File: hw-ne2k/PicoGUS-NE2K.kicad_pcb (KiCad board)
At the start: 2 copper layers, 103.7 x 74.1 mm, 46 parts, among them J1 2x5 header, J2 1x2 header, J3 Bus_ISA_8bit, J5 USB-A, J6 1x2 header, U1 Raspberry Pi Pico W, U10 74LVC2G06, U13 SST39SF010A, U14 74HCT688, U15 74AHCT245, U16 74AHCT1G08, U17 USBLC6-2SC6, U2 74LVC244, U3 SN74CB3T3257, U4 SN74CB3T3257, U5 74AHC14, U6 74LVC00, U7 74LVC1G00, U8 APS6404L-3SQR-SN

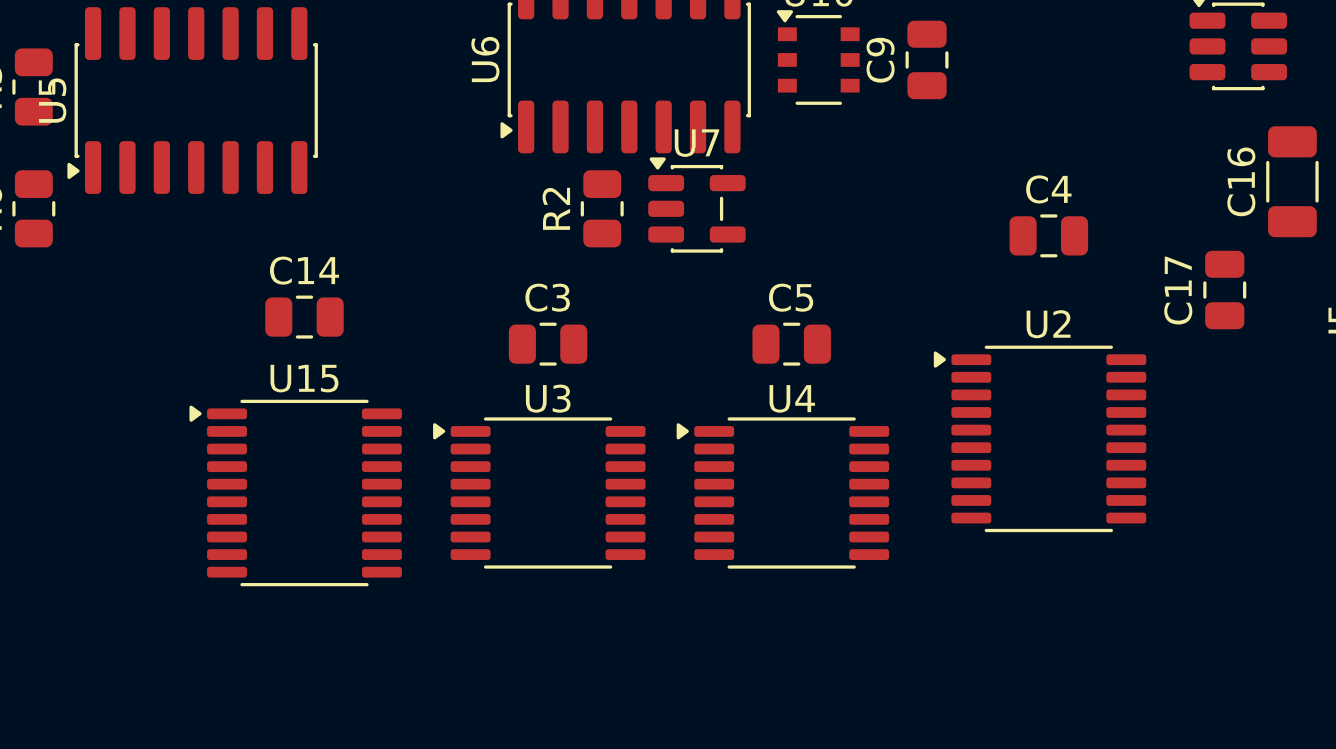
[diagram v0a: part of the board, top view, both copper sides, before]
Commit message: hw-ne2k: bus-switch row moved up/spread for routing escape (board re-routing)
Co-Authored-By: Claude Opus 5.5 <noreply@anthropic.com>
Claude-Session: https://claude.ai/code/session_011utN3x8yYUNDvkpGCEq5yD
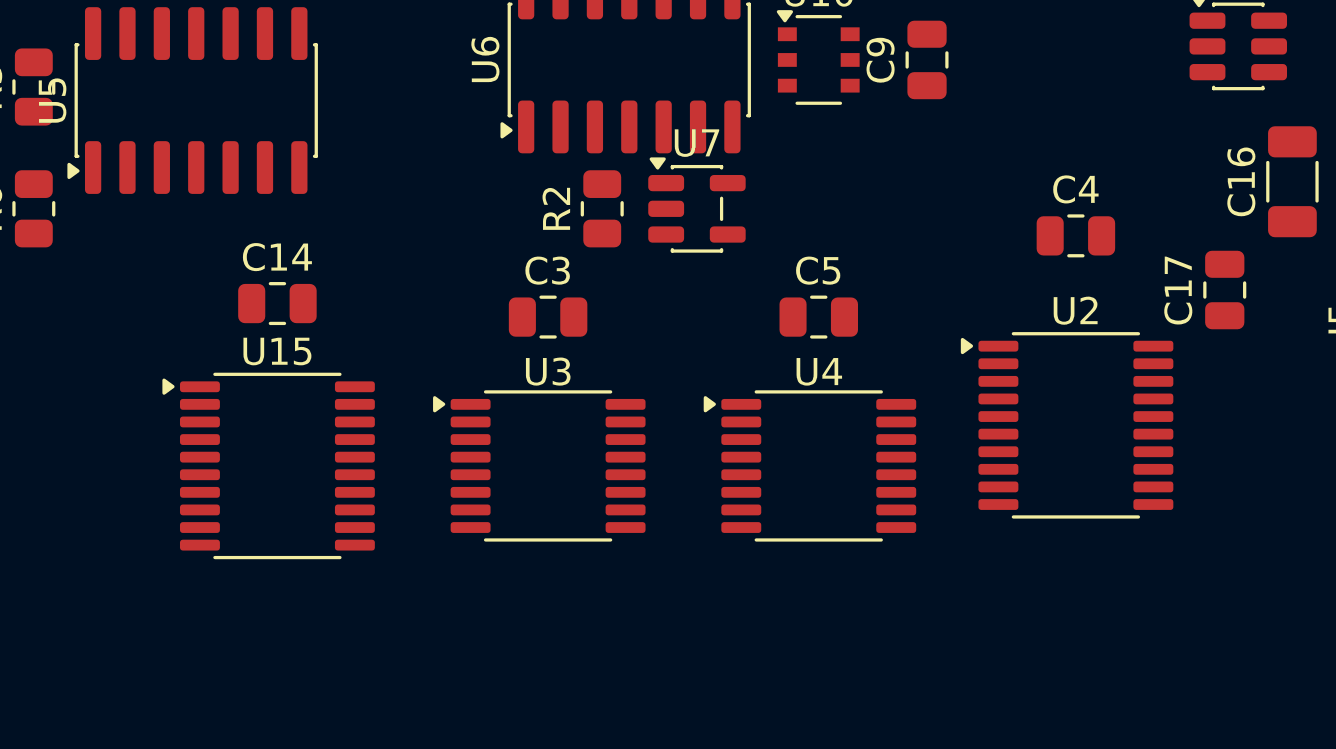
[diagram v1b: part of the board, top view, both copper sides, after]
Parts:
- moved C5 1.41 mm to (185.5, 109.5)
- moved U15 1.41 mm to (165.5, 115.0)
- moved U4 1.41 mm to (185.5, 115.0)
- moved C14 1.12 mm to (165.5, 109.0)
- moved U2 1.12 mm to (195.0, 113.5)
- moved C3 1.00 mm to (175.5, 109.5)
- moved C4 1.00 mm to (195.0, 106.5)
- moved U3 1.00 mm to (175.5, 115.0)

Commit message: hw-ne2k: routed board (DRC 0/0), silkscreen and artwork, README
- Freerouting + manual fix-ups: IRQ grid-routed, GND pour stitched (57
  vias) and U17 GND tied in. KiCad 10 DRC: 0 violations, 0 unconnected,
  schematic parity OK (warnings: 2 silk-to-edge at the USB-A, 3 thermals).
- No copper under the Pico W antenna or between its end and the bracket.
- Front silk: title, IRQ numbers, ROM WE, TX/GND, USB, WiFi antenna, REAR.
  Back: PicoGUS artwork, dedication, copyright/licence (CERN-OHL-P v2).
- README: status, silkscreen, JLCPCB notes (no LCSC numbers yet).

Co-Authored-By: Claude Opus 5.5 <noreply@anthropic.com>
Claude-Session: https://claude.ai/code/session_011utN3x8yYUNDvkpGCEq5yD
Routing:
- net GND: track 0.00 -> 624.3 mm, vias 0 -> 79
- net +5V: track 0.00 -> 282.6 mm, vias 0 -> 11
- net +3V3: track 0.00 -> 173.0 mm, vias 0 -> 5
- net A4: track 0.00 -> 171.9 mm, vias 0 -> 2
- net A6: track 0.00 -> 163.7 mm, vias 0 -> 8
- net IRQ: track 0.00 -> 151.1 mm, vias 0 -> 12
- net A8: track 0.00 -> 144.6 mm, vias 0 -> 9
- net RESET: track 0.00 -> 132.7 mm, vias 0 -> 4
- net ROM_EN: track 0.00 -> 131.9 mm, vias 0 -> 2
- net IRQ2: track 0.00 -> 128.5 mm, vias 0 -> 4
- net A7: track 0.00 -> 123.1 mm, vias 0 -> 8
- net A3: track 0.00 -> 122.0 mm, vias 0 -> 4
- net ROM_BASE0: track 0.00 -> 116.3 mm, vias 0 -> 2
- net A5: track 0.00 -> 111.6 mm, vias 0 -> 6
- net A2: track 0.00 -> 109.0 mm, vias 0 -> 4
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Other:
- board text added: "2/9"
- board text added: "3"
- board text added: "4"
- board text added: "5"
- board text added: "7"
- board text added: "< REAR"
- board text added: "GND"
- board text added: "IRQ"
- board text added: "PicoGUS NE2000"
- board text added: "PicoGUS NE2000 v1.0 © 2023-2026 Ian Scott (polpo), Vidar Waagbø (waagbo) Licensed under CERN-OHL-P v2 https://github.com/waagbo/picogus Thanks to all the people that have contributed over the years!"
- board text added: "REAR >"
- board text added: "ROM WE"
- board text added: "TX"
- board text added: "This version is dedicated to Mila and Alisa, my two wonderful princesses, who fill my world with joy."
- board text added: "USB"
- board text added: "WiFi ANTENNA"
- board text added: "v1.0"

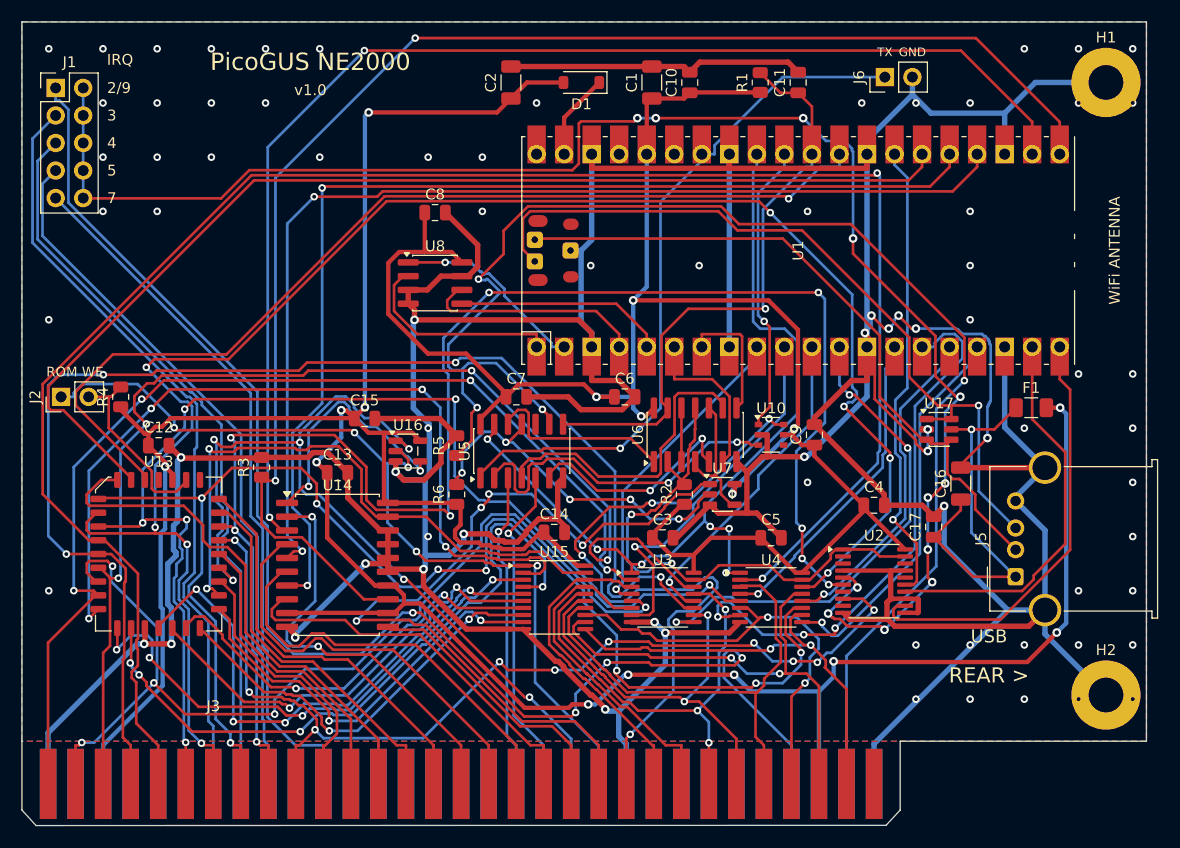
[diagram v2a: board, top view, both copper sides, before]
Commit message: hw-ne2k: user placement, rerouted (DRC 0/0), silkscreen redone
- Placement and reference-label positions from the user's layout kept as-is.
- Freerouting on the new placement: 0 violations, 0 unconnected; GND pour
  stitched (75 vias), one connected GND network.
- Silkscreen: IRQ + 2/9 3 4 5 7 above the J1 columns, ROM WE under J2,
  TX/GND over J6, USB, WiFi antenna, REAR; H1/H2 reference text hidden.
  Back: artwork scaled to 63 mm to clear the Pico and J1 holes.

Co-Authored-By: Claude Opus 5.5 <noreply@anthropic.com>
Claude-Session: https://claude.ai/code/session_011utN3x8yYUNDvkpGCEq5yD
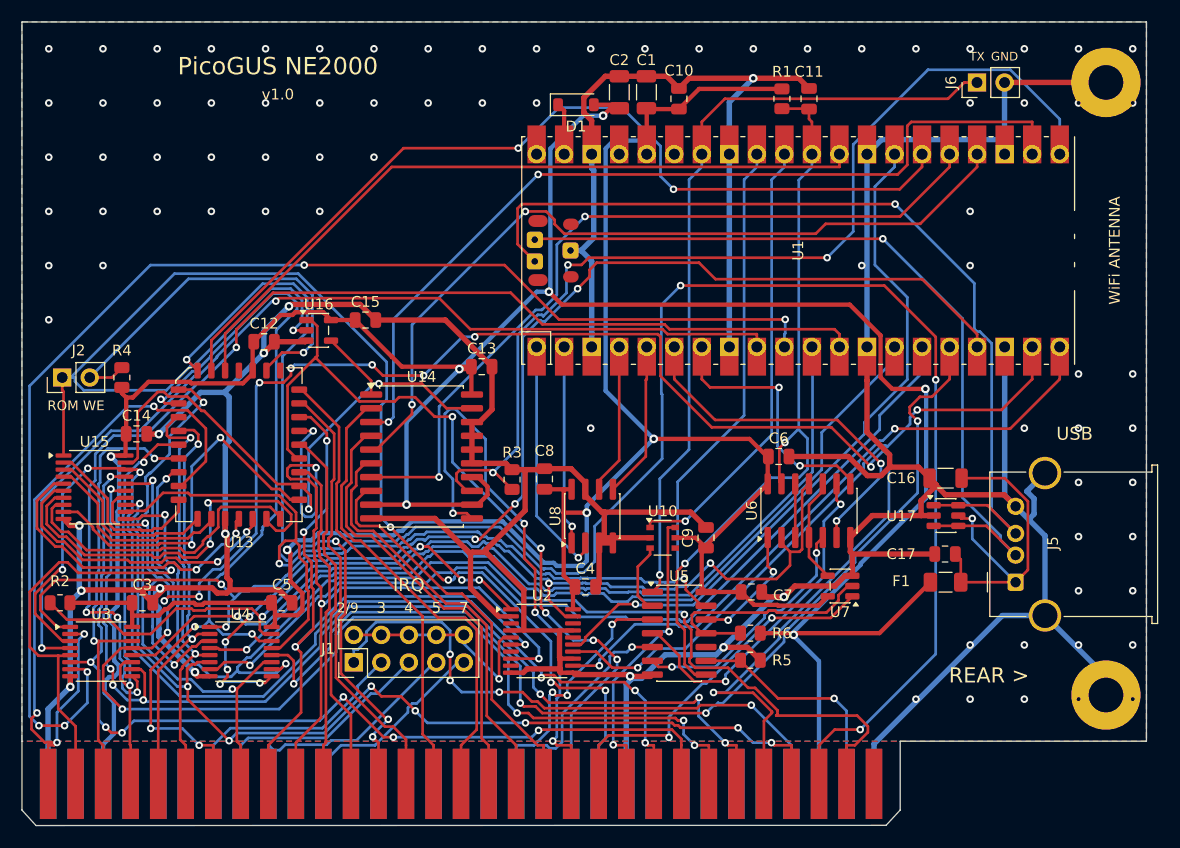
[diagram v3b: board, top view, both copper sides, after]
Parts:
- moved J1 59.7 mm to (147.0, 121.0), turned to 90 degrees
- moved R2 58.5 mm to (119.9, 115.5), turned to 180 degrees
- moved U3 52.0 mm to (123.7, 120.0)
- moved U4 49.2 mm to (136.6, 120.0)
- moved C3 48.4 mm to (127.5, 115.5)
- moved C5 45.5 mm to (140.4, 115.5)
- moved U15 43.6 mm to (123.1, 104.8)
- moved C14 39.6 mm to (127.0, 99.9)
- moved R5 33.6 mm to (183.6, 120.8), turned to 0 degrees
- moved U2 31.1 mm to (164.4, 119.0)
- moved R6 30.0 mm to (183.6, 118.3), turned to 180 degrees
- moved C7 28.2 mm to (183.7, 114.5)
- moved C4 27.7 mm to (168.4, 114.0)
- moved C8 26.6 mm to (164.6, 104.1), turned to 90 degrees
- moved U8 25.9 mm to (169.0, 107.5), turned to 90 degrees
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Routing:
- net A4: track 171.9 -> 38.4 mm
- net IRQ: track 151.1 -> 20.2 mm, vias 12 -> 1
- net D6: track 44.3 -> 169.6 mm, vias 2 -> 4
- net D4: track 45.3 -> 165.9 mm, vias 0 -> 11
- net RESET: track 132.7 -> 21.7 mm, vias 4 -> 1
- net GND: track 624.3 -> 522.4 mm, vias 79 -> 88
- net AD1: track 34.4 -> 120.6 mm, vias 1 -> 5
- net A3: track 122.0 -> 38.6 mm, vias 4 -> 2
- net A6: track 163.7 -> 81.1 mm, vias 8 -> 5
- net A8: track 144.6 -> 65.2 mm, vias 9 -> 4
- net D0: track 29.5 -> 107.8 mm, vias 0 -> 6
- net IRQ2: track 128.5 -> 54.3 mm
- net A5: track 111.6 -> 39.8 mm, vias 6 -> 2
- net A7: track 123.1 -> 51.8 mm, vias 8 -> 2
- net AD7: track 36.2 -> 106.6 mm, vias 1 -> 8
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
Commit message: hw-ne2k: placement proposal (unrouted): bus switches + ROM buffer at the data fingers
U3/U4 (CB3T3257) and U15 (ROM data buffer) move next to D0-D7 to keep the
ISA data lines short; U2 moves left next to J1 / A8-A9, U5 + C7 and R5/R6
shift left of the new row. Everything else as in the user's layout.
Routing stripped for review (routed version: 28f17e1).

Co-Authored-By: Claude Opus 5.5 <noreply@anthropic.com>
Claude-Session: https://claude.ai/code/session_011utN3x8yYUNDvkpGCEq5yD
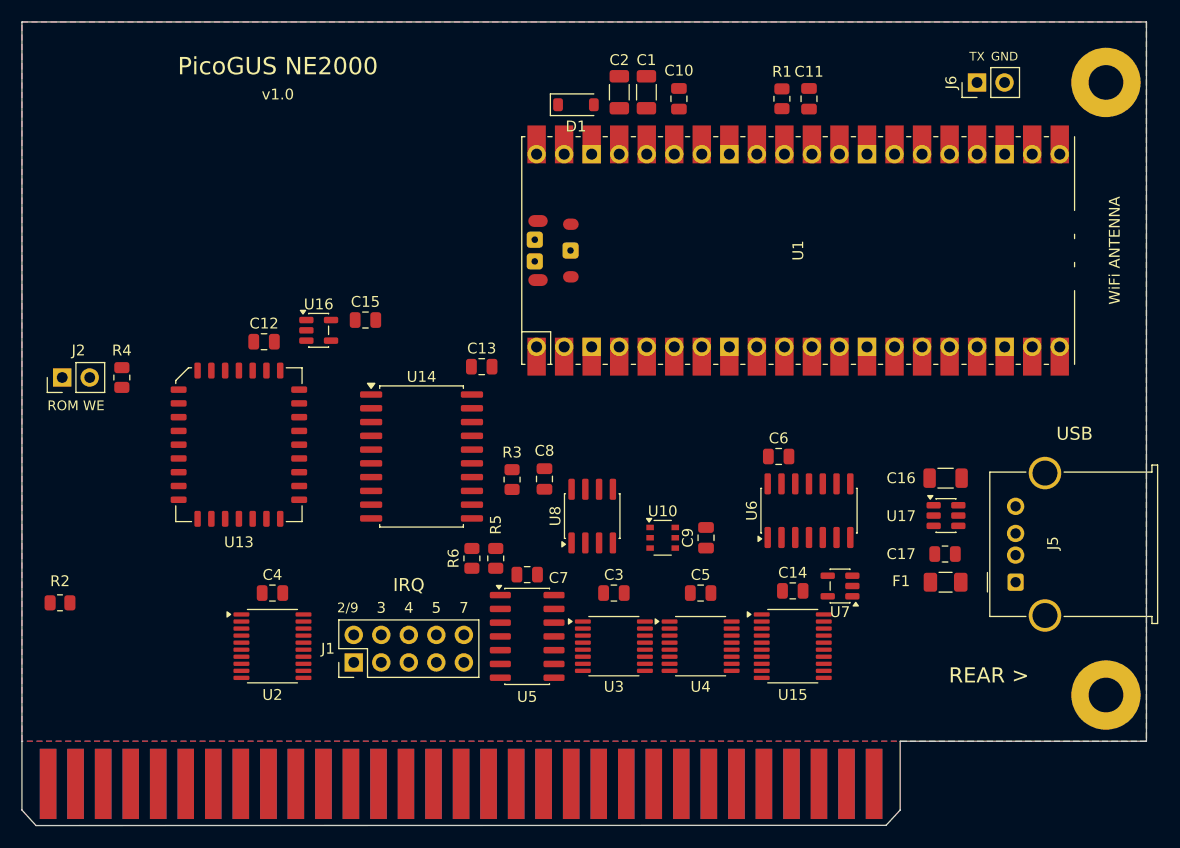
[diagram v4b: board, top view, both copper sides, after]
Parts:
- moved U15 66.1 mm to (187.5, 119.5)
- moved C14 62.3 mm to (187.5, 114.4)
- moved U3 47.3 mm to (171.0, 119.5)
- moved C3 43.5 mm to (171.0, 114.6)
- moved U4 42.4 mm to (179.0, 119.5)
- moved C5 38.6 mm to (179.0, 114.6)
- moved C4 28.9 mm to (139.5, 114.6)
- moved R6 26.6 mm to (157.9, 111.4), turned to 90 degrees
- moved R5 25.3 mm to (160.1, 111.4), turned to 90 degrees
- moved U2 24.9 mm to (139.5, 119.5)
- moved C7 20.7 mm to (163.0, 112.9)
- moved U5 14.0 mm to (163.0, 118.6)
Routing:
- net GND: track 522.4 -> 0.00 mm, vias 88 -> 0
- net +5V: track 247.9 -> 0.00 mm, vias 7 -> 0
- net +3V3: track 186.8 -> 0.00 mm, vias 3 -> 0
- net D6: track 169.6 -> 0.00 mm, vias 4 -> 0
- net D4: track 165.9 -> 0.00 mm, vias 11 -> 0
- net ~{SMEMW}: track 128.8 -> 0.00 mm, vias 5 -> 0
- net ADS: track 120.8 -> 0.00 mm, vias 3 -> 0
- net AD1: track 120.6 -> 0.00 mm, vias 5 -> 0
- net D7: track 108.4 -> 0.00 mm, vias 3 -> 0
- net D0: track 107.8 -> 0.00 mm, vias 6 -> 0
- net AD3: track 106.7 -> 0.00 mm, vias 4 -> 0
- net AD7: track 106.6 -> 0.00 mm, vias 8 -> 0
- net ~{BUSOE}: track 106.5 -> 0.00 mm, vias 6 -> 0
- net D2: track 100.0 -> 0.00 mm, vias 6 -> 0
- net D3: track 97.5 -> 0.00 mm, vias 7 -> 0
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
